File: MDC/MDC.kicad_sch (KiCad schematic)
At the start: 23 parts, among them IC1 ADUM121N1BRZ, IC2 MCP2551-E_SN, J1 ENC_L, J2 ENC_R, J3 JetsonGPIO, J4 Conn_01x04, J5 MD, U1 NUCLEO-F303K8

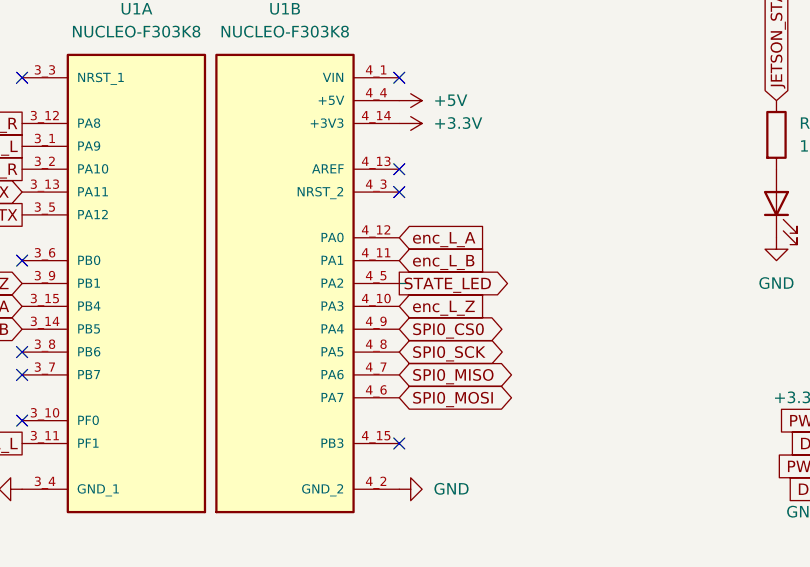
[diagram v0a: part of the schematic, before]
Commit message: 非常停止スイッチを追加
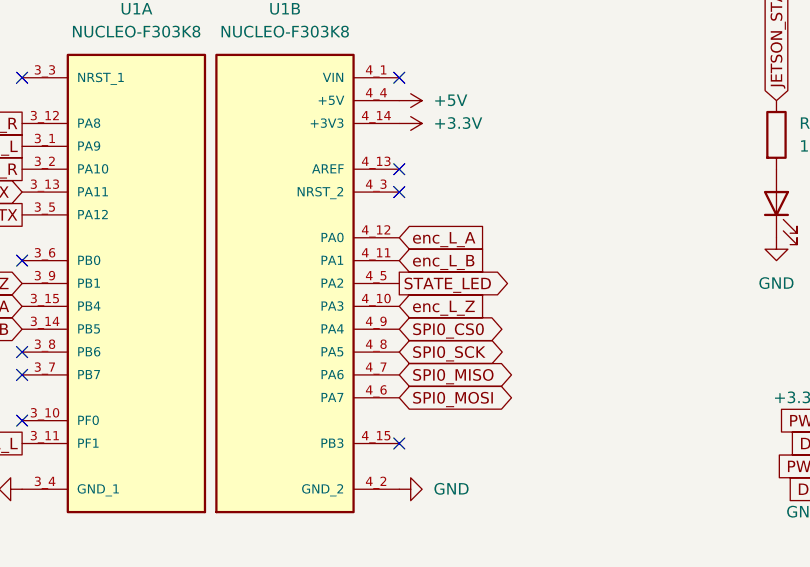
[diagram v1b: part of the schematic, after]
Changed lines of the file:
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@@
-	(wire
-		(pts
-			(xy 204.47 62.23) (xy 203.2 62.23)
-		)
-		(stroke
-			(width 0)
-			(type default)
-		)
-	)
 	(wire
 		(pts
